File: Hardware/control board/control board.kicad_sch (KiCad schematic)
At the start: 9 parts, among them J1 Conn_01x03_Pin, J2 Conn_01x03_Pin, J3 Conn_01x03_Pin, J4 Conn_01x03_Pin, J5 Conn_01x03_Pin, J6 Conn_01x03_Pin, J7 Conn_01x03_Pin, J8 Conn_01x03_Pin

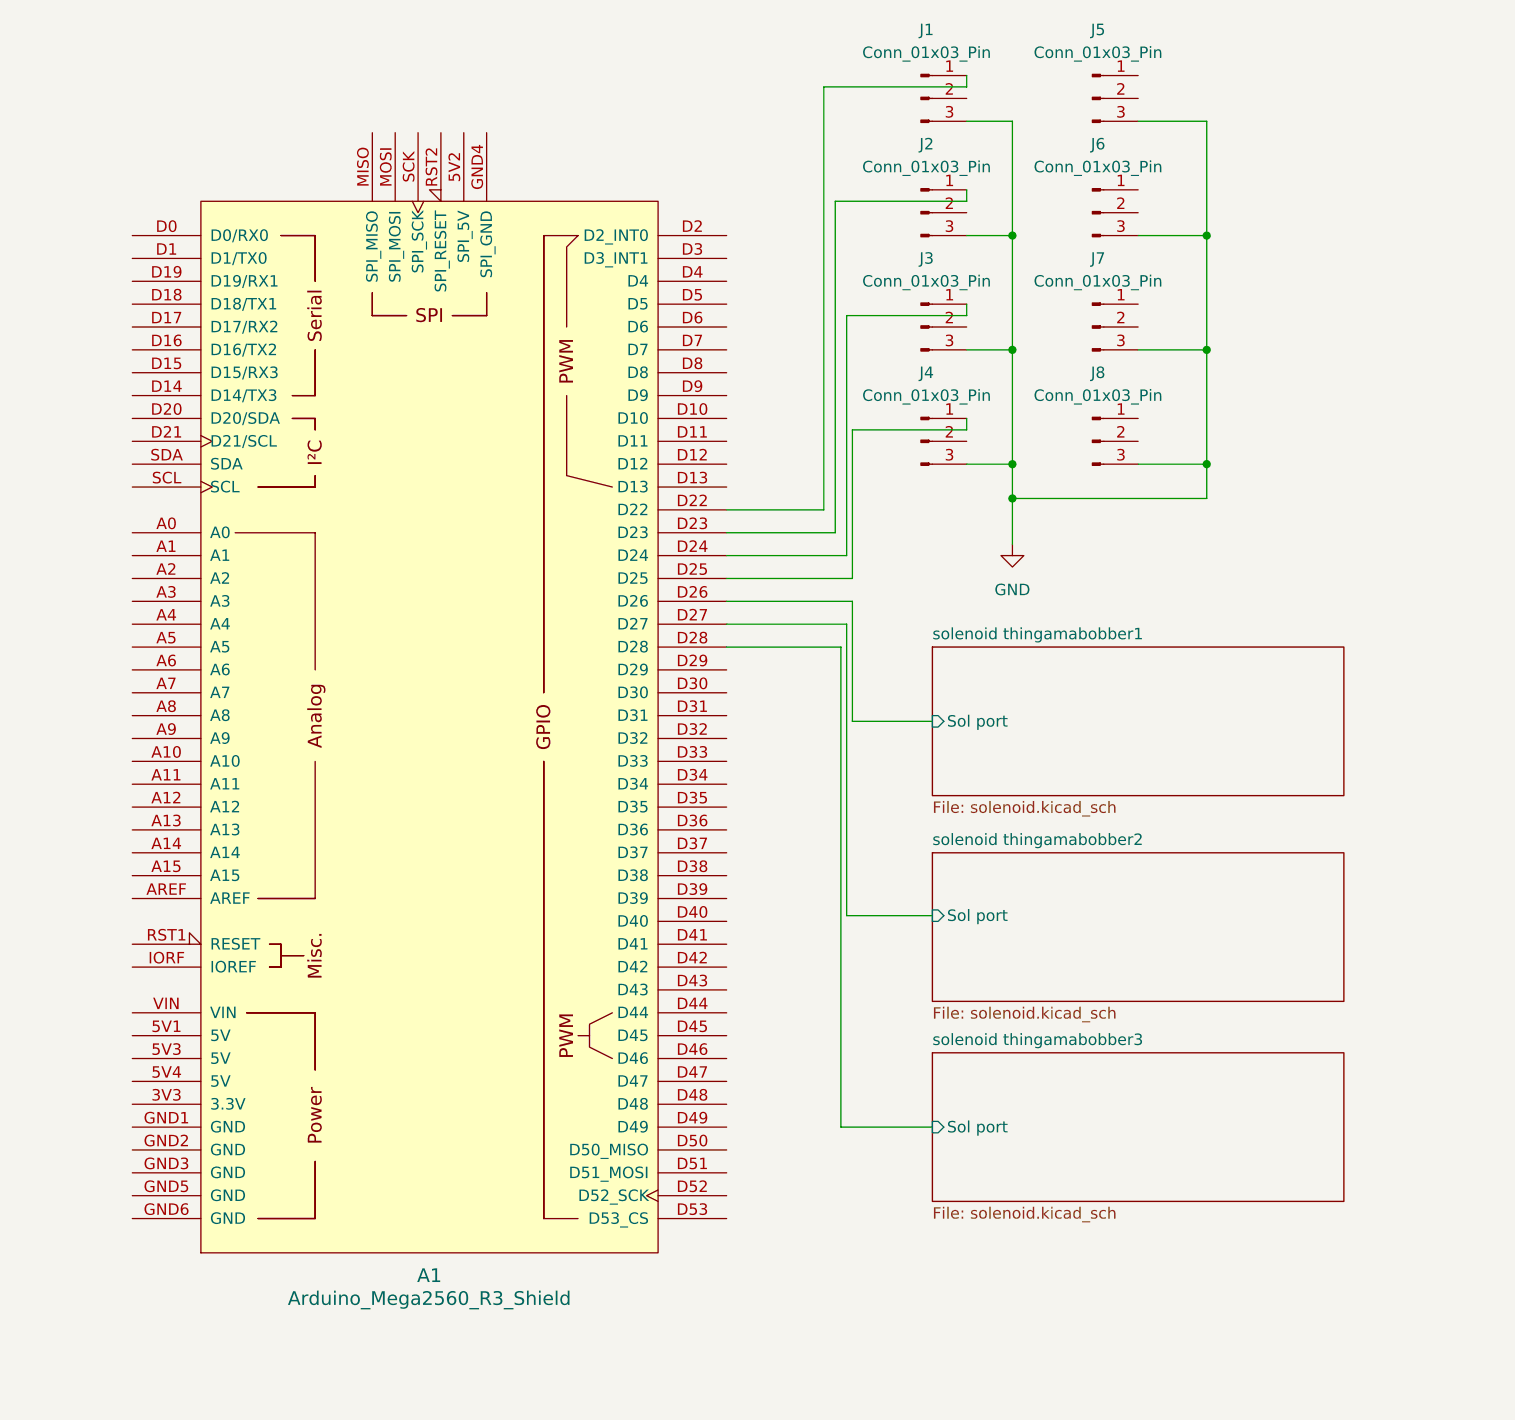
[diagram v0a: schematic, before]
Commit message: added fuses into solenoids/escs
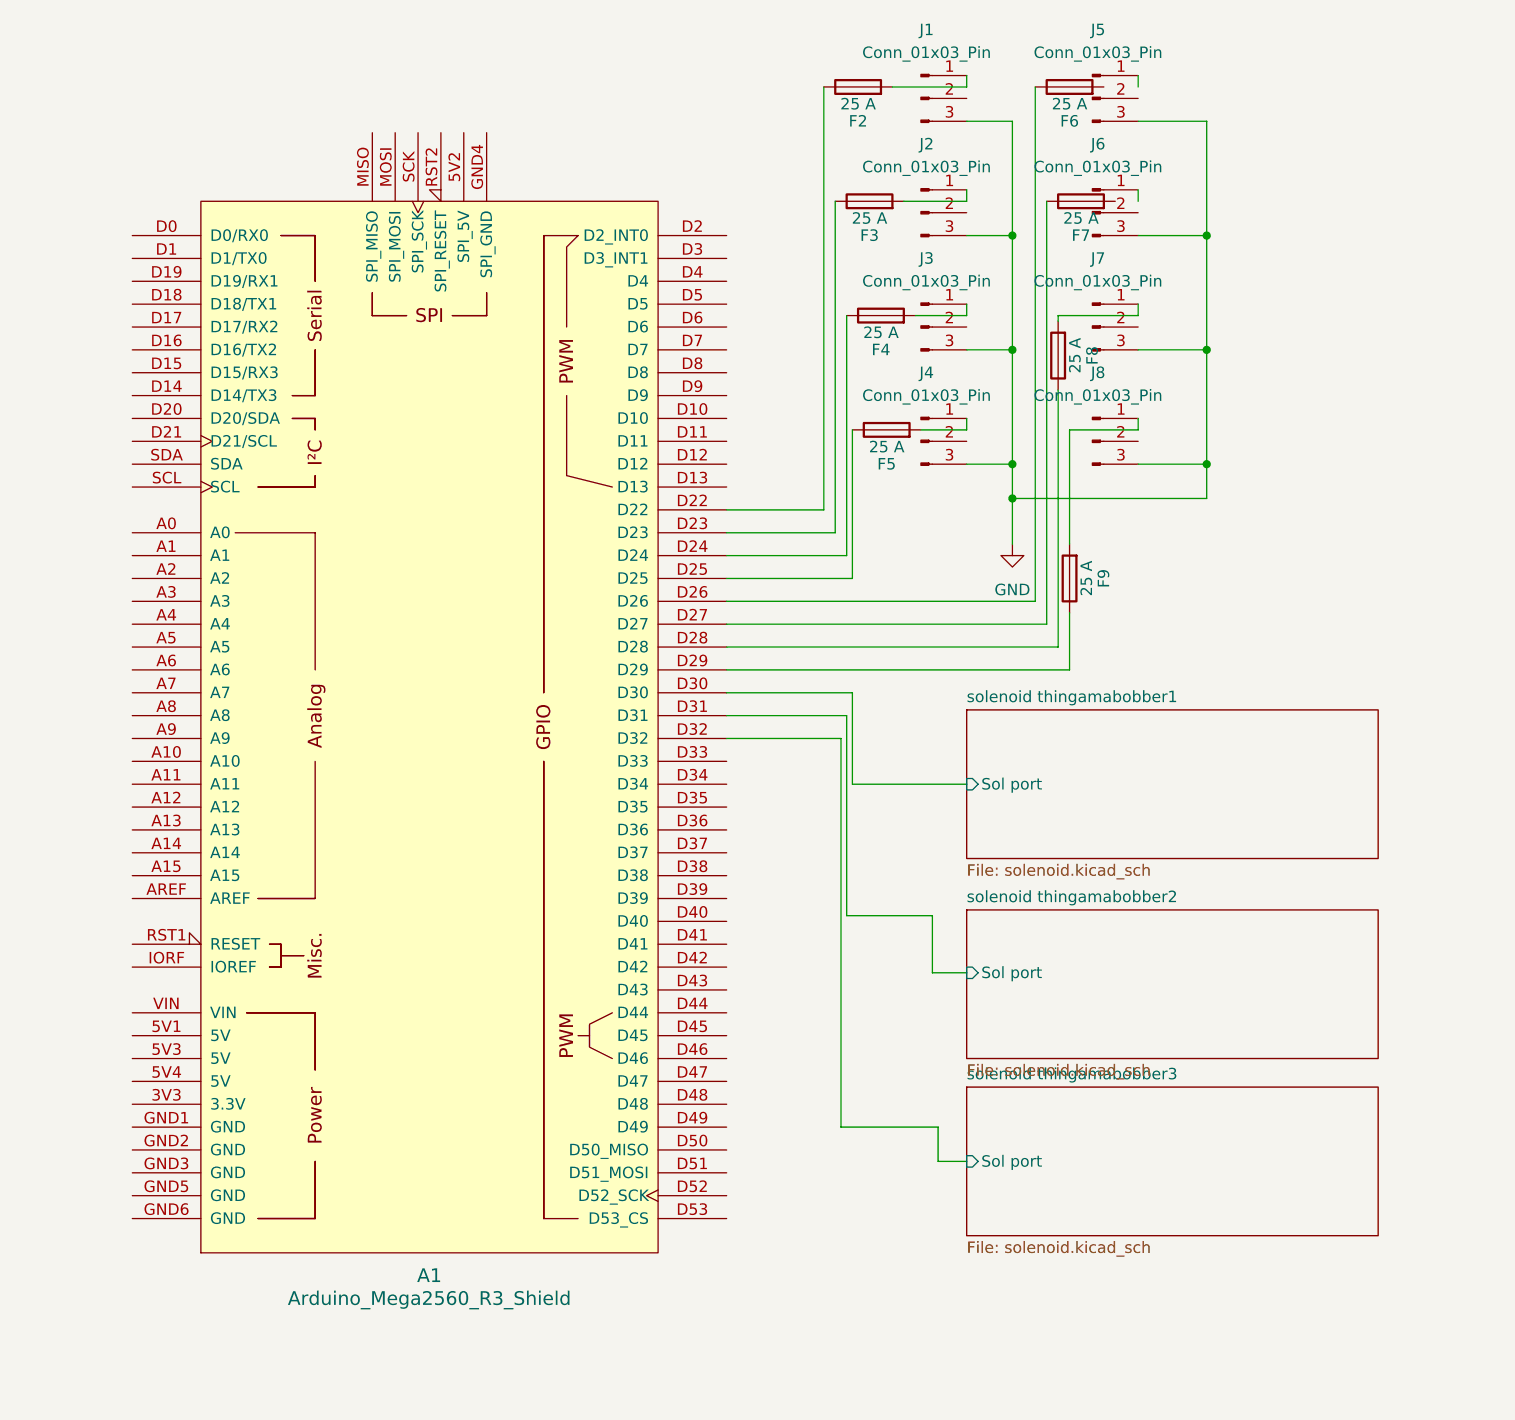
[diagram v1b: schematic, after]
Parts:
- added F2, F3, F4, F5, F6, F7, F8, F9: 25 A, symbol Device:Fuse
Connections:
- net solenoid thingamabobber1/Sol port: now also A1.D30; no longer A1.D26
- net solenoid thingamabobber2/Sol port: now also A1.D31; no longer A1.D27
- net solenoid thingamabobber3/Sol port: now also A1.D32; no longer A1.D28
- net at A1.D22: now also F2.1; no longer J1.1 (Pin_1)
- net at A1.D23: now also F3.1; no longer J2.1 (Pin_1)
- net at A1.D24: now also F4.1; no longer J3.1 (Pin_1)
- net at A1.D25: now also F5.1; no longer J4.1 (Pin_1)
- net at A1.D29: now also F9.1
- net at J8.1 (Pin_1): now also F9.2
- net at J7.1 (Pin_1): now also F8.2
- new net: F2.2, J1.1 (Pin_1)
- new net: F5.2, J4.1 (Pin_1)
- new net: A1.D26, F6.1
- new net: A1.D27, F7.1
- new net: A1.D28, F8.1
- new net: F4.2, J3.1 (Pin_1)
- new net: F3.2, J2.1 (Pin_1)

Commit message: renamed boards
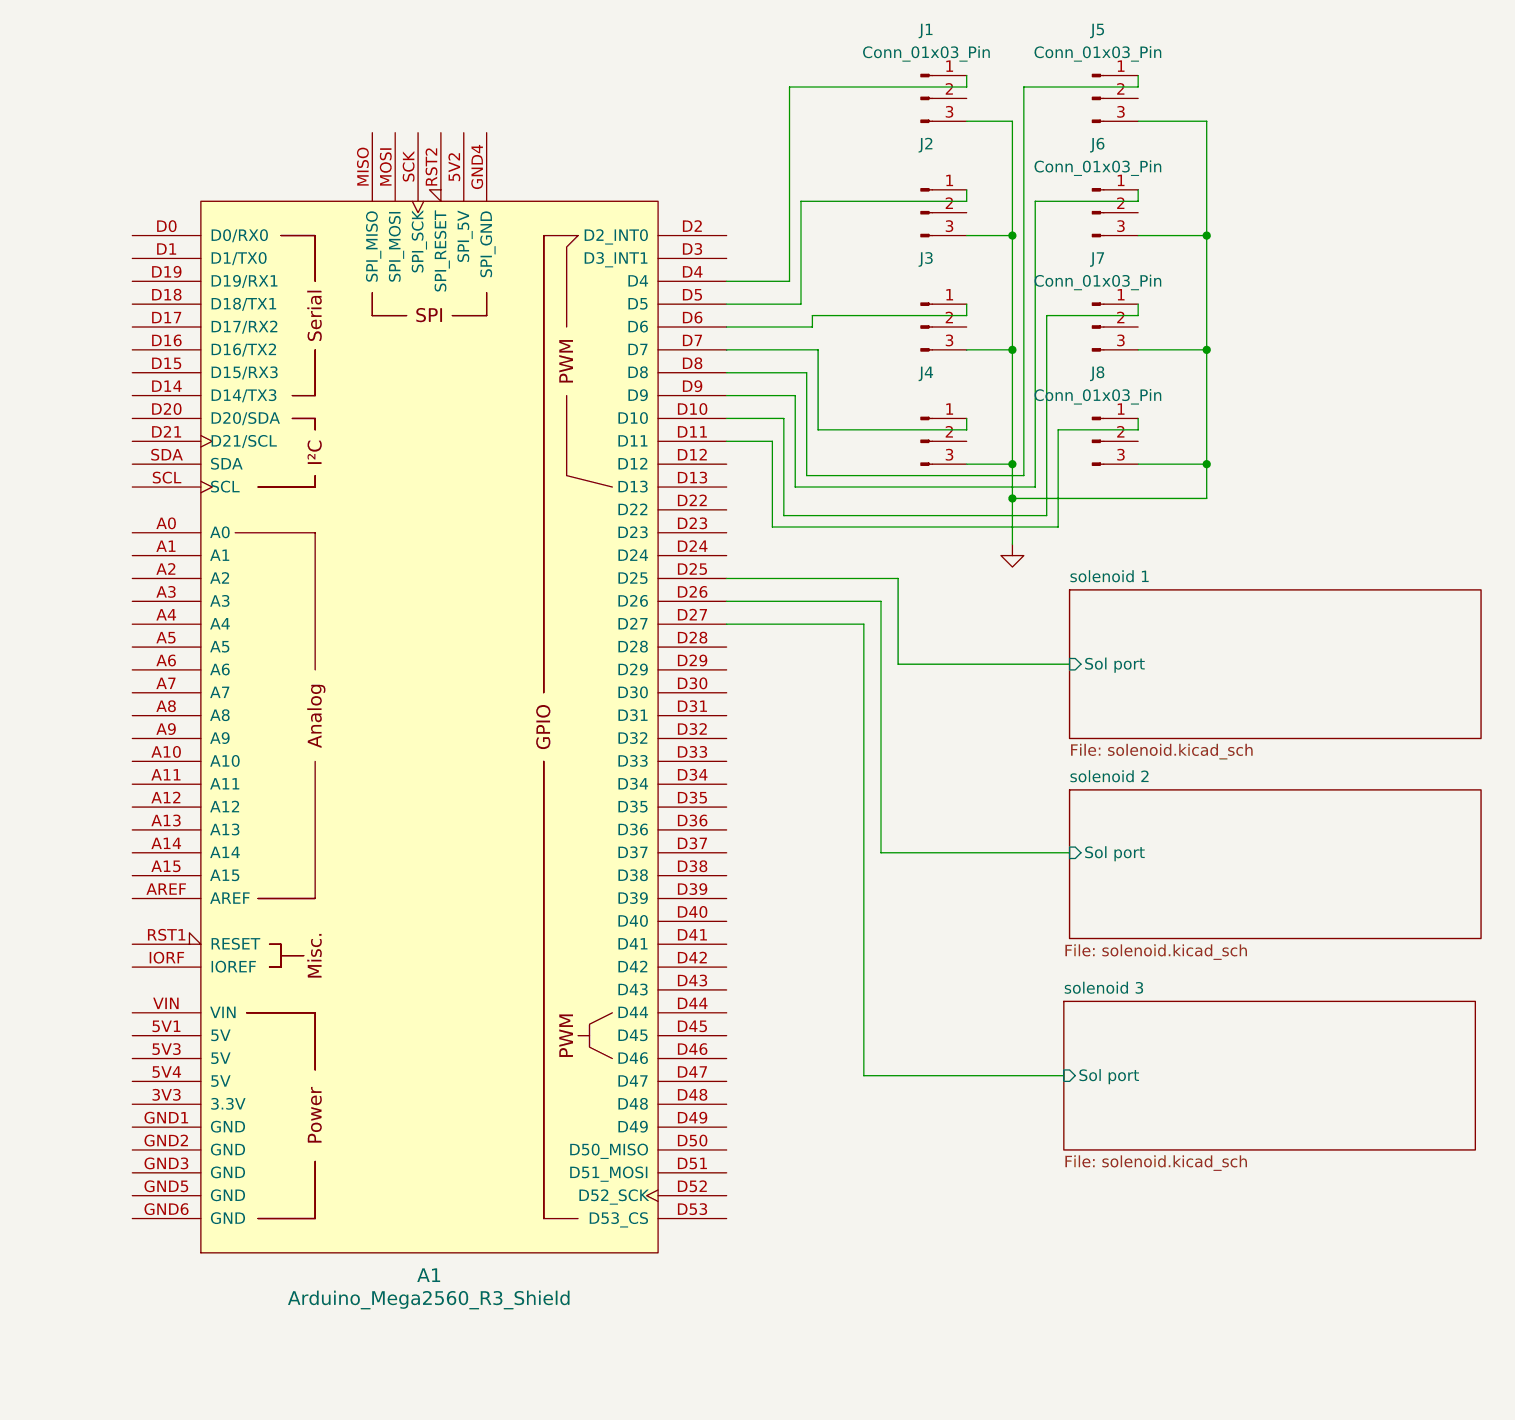
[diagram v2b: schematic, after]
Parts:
- removed F2, F3, F4, F5, F6, F7, F8, F9: 25 A, symbol Device:Fuse
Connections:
- net solenoid 1/Sol port: now also A1.D25; no longer A1.D30
- net solenoid 2/Sol port: now also A1.D26; no longer A1.D31
- net solenoid 3/Sol port: now also A1.D27; no longer A1.D32
- net at J1.1 (Pin_1): now also A1.D4
- net at J4.1 (Pin_1): now also A1.D7
- net at A1.D10: now also J7.1 (Pin_1)
- net at A1.D11: now also J8.1 (Pin_1)
- net at A1.D5: now also J2.1 (Pin_1)
- net at A1.D6: now also J3.1 (Pin_1)
- net at A1.D8: now also J5.1 (Pin_1)
- net at A1.D9: now also J6.1 (Pin_1)
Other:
- sheet solenoid thingamabobber1 renamed solenoid 1
- sheet solenoid thingamabobber2 renamed solenoid 2
- sheet solenoid thingamabobber3 renamed solenoid 3
